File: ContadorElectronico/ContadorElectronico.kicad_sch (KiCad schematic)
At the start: 21 parts, among them J7 INPUT, J8 POWER, SW1 MODE, SW2 INC, SW3 DEC, U3 4N35, U4 4N35

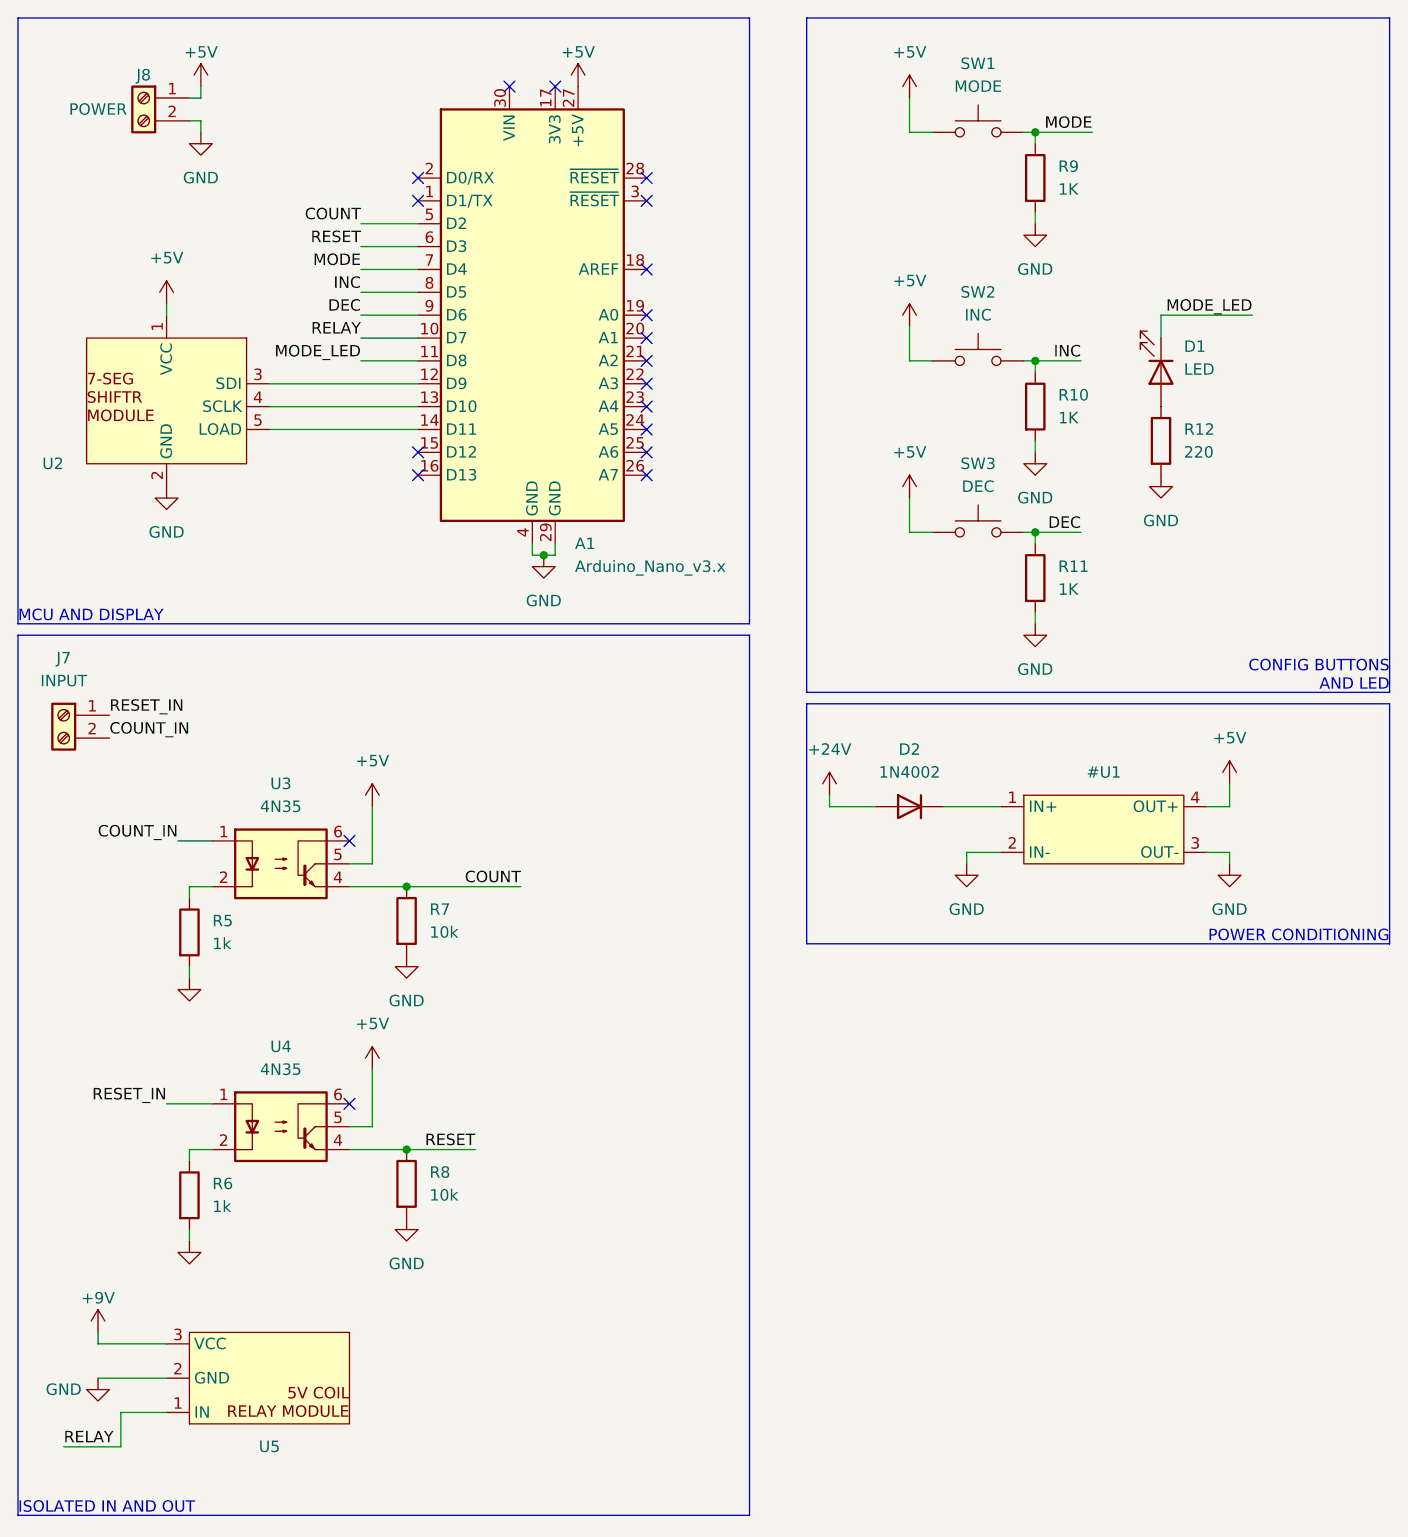
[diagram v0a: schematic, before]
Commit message: PCB design with 3 pin bornier
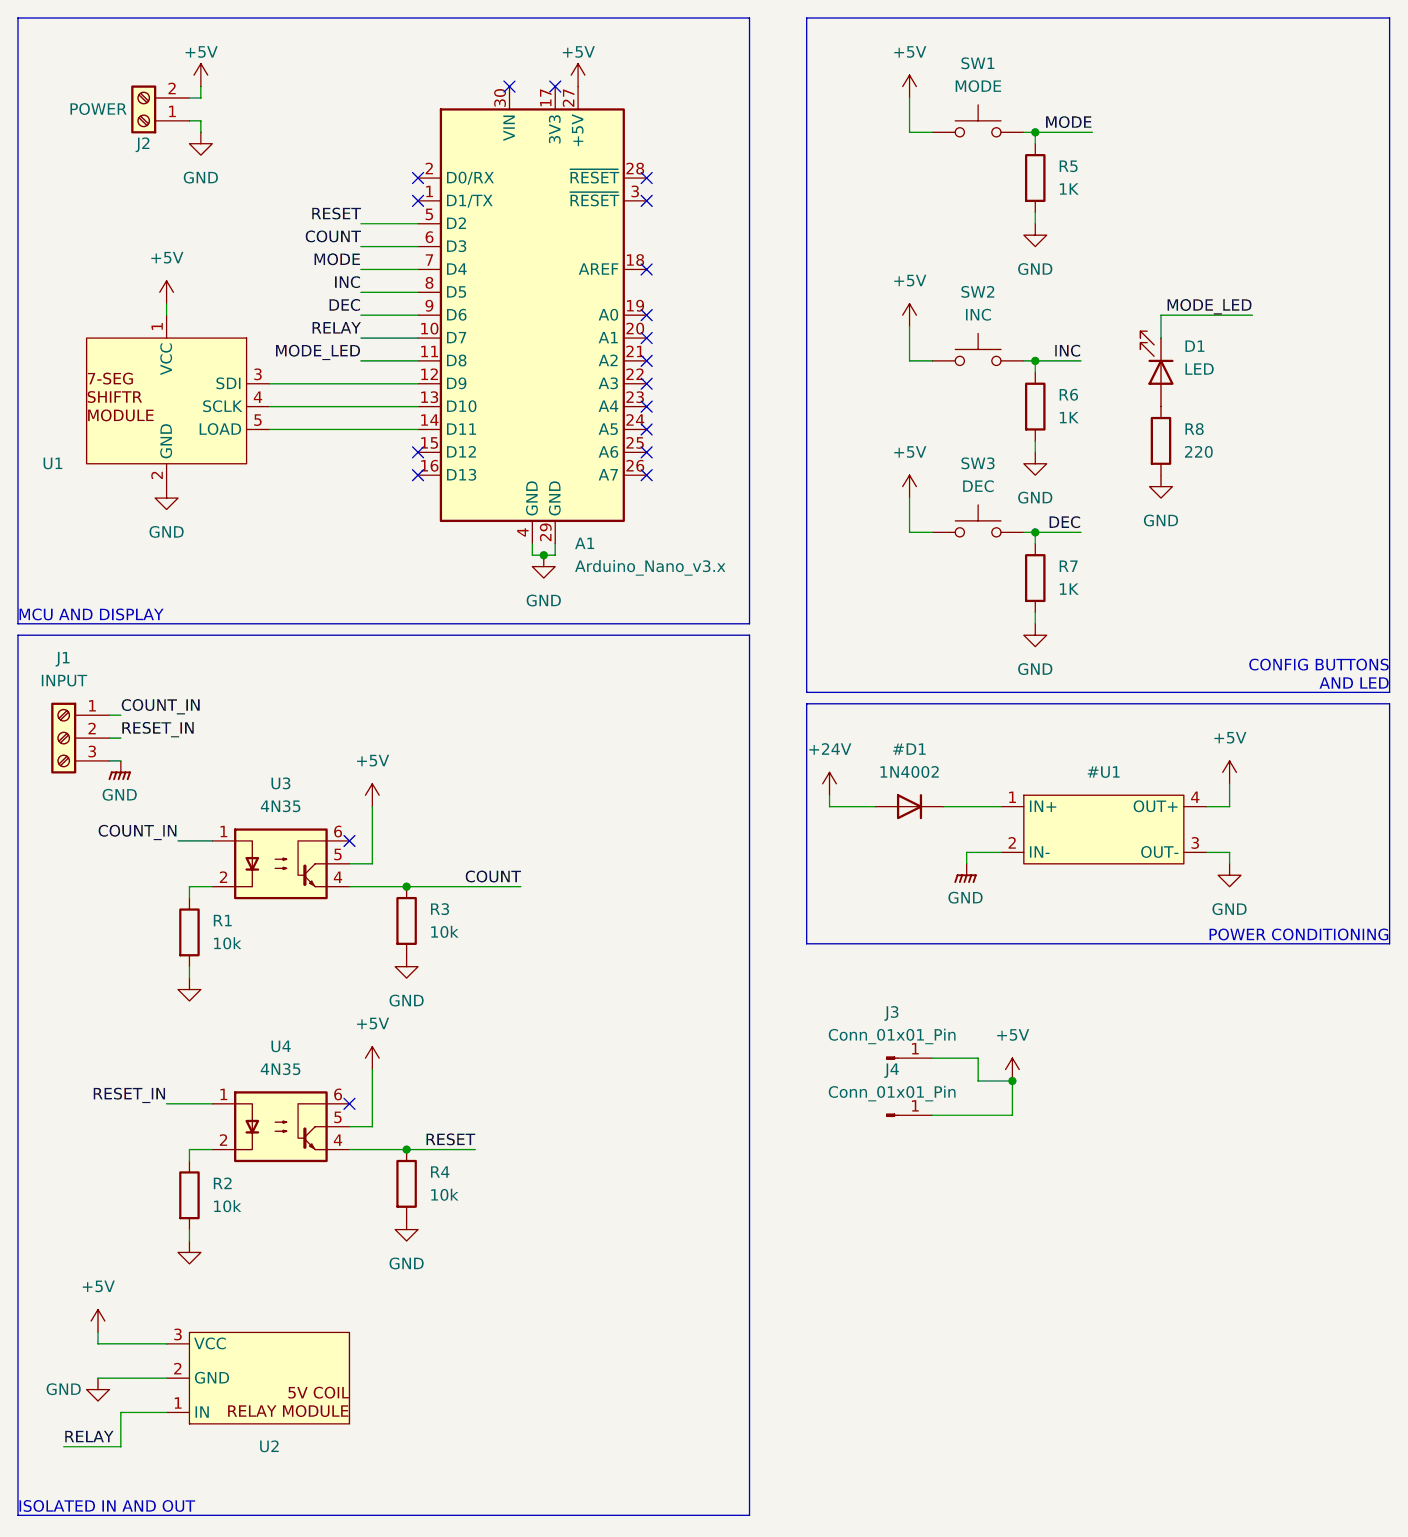
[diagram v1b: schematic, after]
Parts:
- added J3, J4: Conn_01x01_Pin, Connector_Pin:Pin_D1.3mm_L11.3mm_W2.8mm_Flat, symbol Connector:Conn_01x01_Pin
- D1, SW1, SW2, SW3: footprint Connector_PinSocket_2.54mm:PinSocket_1x02_P2.54mm_Vertical -> Connector_PinHeader_2.54mm:PinHeader_1x02_P2.54mm_Vertical
- J1: renamed from J7; footprint TerminalBlock:TerminalBlock_bornier-2_P5.08mm -> TerminalBlock:TerminalBlock_bornier-3_P5.08mm; symbol Connector:Screw_Terminal_01x02 -> Connector:Screw_Terminal_01x03
- R1: renamed from R5; value 1k -> 10k
- R2: renamed from R6; value 1k -> 10k
- U1: renamed from U2; footprint Connector_PinSocket_2.54mm:PinSocket_1x05_P2.54mm_Vertical -> Connector_PinHeader_2.54mm:PinHeader_1x05_P2.54mm_Vertical
- U2: renamed from U5; footprint Connector_PinSocket_2.54mm:PinSocket_1x03_P2.54mm_Vertical -> Connector_PinHeader_2.54mm:PinHeader_1x03_P2.54mm_Vertical
- U3, U4: footprint Package_DIP:DIP-6_W7.62mm -> Package_DIP:DIP-6_W7.62mm_Socket
- renumbered D2 to #D1, J8 to J2, R7 to R3, R8 to R4, R9 to R5, R10 to R6, R11 to R7, R12 to R8
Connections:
- net +9V is gone; now on net +5V: U2.3 (VCC)
- net +5V: now also J2.2 (Pin_2), J3.1 (Pin_1), J4.1 (Pin_1); no longer J2.1 (Pin_1)
- net COUNT: now also A1.6 (D3); no longer A1.5 (D2)
- net COUNT_IN: now also J1.1 (Pin_1); no longer J1.2 (Pin_2)
- net GND: now also J2.1 (Pin_1); no longer #U1.2 (IN-), J2.2 (Pin_2)
- net RESET: now also A1.5 (D2); no longer A1.6 (D3)
- net RESET_IN: now also J1.2 (Pin_2); no longer J1.1 (Pin_1)
- new net GNDPWR: #U1.2 (IN-), J1.3 (Pin_3)
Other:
- moved on the sheet: J2

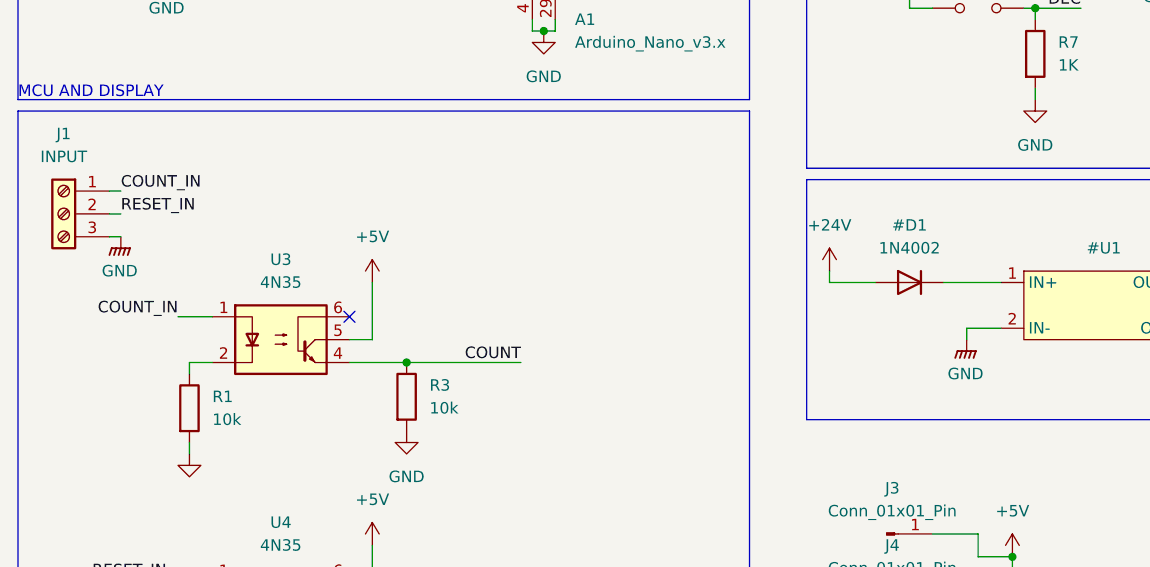
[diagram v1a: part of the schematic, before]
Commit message: 2 Pin Bornier for inputs
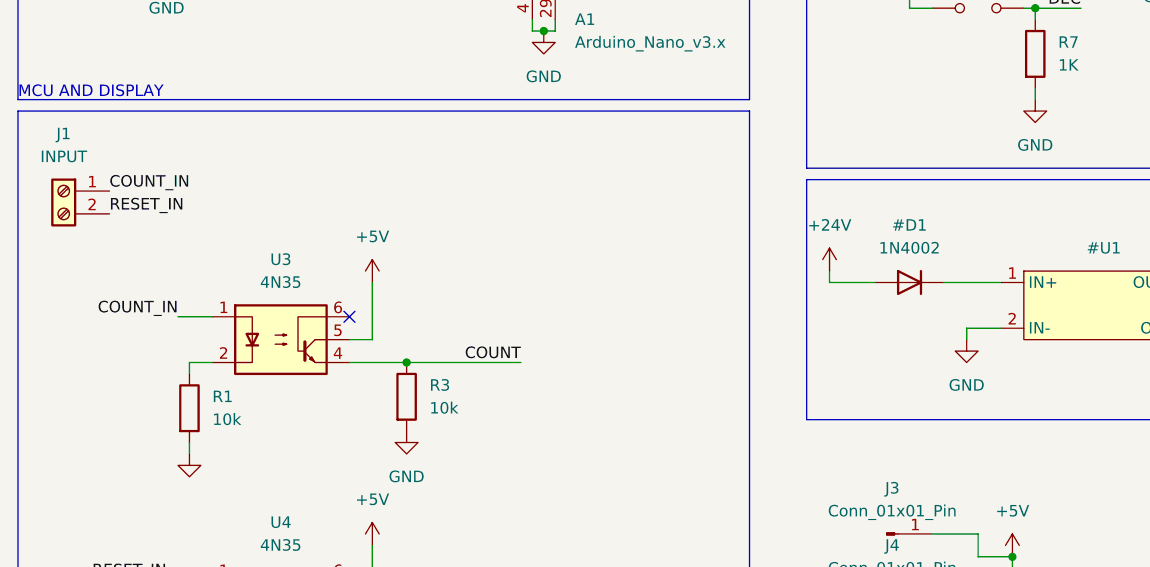
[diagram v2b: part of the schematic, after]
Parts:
- J1: footprint TerminalBlock:TerminalBlock_bornier-3_P5.08mm -> TerminalBlock:TerminalBlock_bornier-2_P5.08mm; symbol Connector:Screw_Terminal_01x03 -> Connector:Screw_Terminal_01x02
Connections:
- net GND: now also #U1.2 (IN-)
- removed net GNDPWR: #U1.2 (IN-), J1.3 (Pin_3)
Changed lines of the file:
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@@
-    (stroke (width 0) (type default))
-  )
-  (wire (pts (xy 31.75 99.06) (xy 30.48 99.06))
     (stroke (width 0) (type default))
   )
@@
     (stroke (width 0) (type default))
   )
-  (wire (pts (xy 31.75 101.6) (xy 30.48 101.6))
-    (stroke (width 0) (type default))
-  )
   (wire (pts (xy 123.19 106.68) (xy 129.54 106.68))
     (stroke (width 0) (type default))
@@
   )
   (wire (pts (xy 29.21 166.37) (xy 29.21 165.1))
-    (stroke (width 0) (type default))
-  )
-  (wire (pts (xy 31.75 96.52) (xy 30.48 96.52))
     (stroke (width 0) (type default))
   )
@@
     (effects (font (size 1.27 1.27)) (justify right bottom))
   )
-  (label "COUNT_IN" (at 31.75 96.52 0) (fields_autoplaced)
+  (label "COUNT_IN" (at 30.48 96.52 0) (fields_autoplaced)
     (effects (font (size 1.27 1.27)) (justify left bottom))
   )
@@
     (effects (font (size 1.27 1.27)) (justify right bottom))
   )
-  (label "RESET_IN" (at 31.75 99.06 0) (fields_autoplaced)
+  (label "RESET_IN" (at 30.48 99.06 0) (fields_autoplaced)
     (effects (font (size 1.27 1.27)) (justify left bottom))
   )
@@
     )
   )
-  (symbol (lib_id "power:GNDPWR") (at 125.73 113.03 0) (unit 1)
+  (symbol (lib_id "power:GND") (at 125.73 113.03 0) (unit 1)
     (in_bom yes) (on_board yes) (dnp no) (fields_autoplaced)
     (property "Reference" "#PWR019" (at 125.73 119.38 0)
       (effects (font (size 1.27 1.27)) hide)
     )
-    (property "Value" "GND" (at 125.603 116.84 0)
-      (effects (font (size 1.27 1.27)))
-    )
-    (property "Footprint" "" (at 125.73 114.3 0)
-      (effects (font (size 1.27 1.27)) hide)
-    )
-    (property "Datasheet" "" (at 125.73 114.3 0)
+    (property "Value" "GND" (at 125.73 118.11 0)
+      (effects (font (size 1.27 1.27)))
+    )
+    (property "Footprint" "" (at 125.73 113.03 0)
+      (effects (font (size 1.27 1.27)) hide)
+    )
+    (property "Datasheet" "" (at 125.73 113.03 0)
       (effects (font (size 1.27 1.27)) hide)
     )
@@
     )
   )
-  (symbol (lib_id "Connector:Screw_Terminal_01x03") (at 25.4 99.06 0) (mirror y) (unit 1)
+  (symbol (lib_id "Connector:Screw_Terminal_01x02") (at 25.4 96.52 0) (mirror y) (unit 1)
     (in_bom yes) (on_board yes) (dnp no) (fields_autoplaced)
     (property "Reference" "J1" (at 25.4 90.17 0)
@@
       (effects (font (size 1.27 1.27)))
     )
-    (property "Footprint" "TerminalBlock:TerminalBlock_bornier-3_P5.08mm" (at 25.4 99.06 0)
-      (effects (font (size 1.27 1.27)) hide)
-    )
-    (property "Datasheet" "~" (at 25.4 99.06 0)
-      (effects (font (size 1.27 1.27)) hide)
-    )
-    (pin "1")
-    (pin "2")
-    (pin "3")
+    (property "Footprint" "TerminalBlock:TerminalBlock_bornier-2_P5.08mm" (at 25.4 96.52 0)
+      (effects (font (size 1.27 1.27)) hide)
+    )
+    (property "Datasheet" "~" (at 25.4 96.52 0)
+      (effects (font (size 1.27 1.27)) hide)
+    )
+    (pin "1")
+    (pin "2")
     (instances
       (project "ContadorElectronico"
@@
         )
       )
-    )
-  )
-  (symbol (lib_id "power:GNDPWR") (at 31.75 101.6 0) (unit 1)
-    (in_bom yes) (on_board yes) (dnp no) (fields_autoplaced)
-    (property "Reference" "#PWR027" (at 31.75 107.95 0)
-      (effects (font (size 1.27 1.27)) hide)
-    )
-    (property "Value" "GND" (at 31.623 105.41 0)
-      (effects (font (size 1.27 1.27)))
-    )
-    (property "Footprint" "" (at 31.75 102.87 0)
-      (effects (font (size 1.27 1.27)) hide)
-    )
-    (property "Datasheet" "" (at 31.75 102.87 0)
-      (effects (font (size 1.27 1.27)) hide)
-    )
-    (pin "1")
-    (instances
-      (project "ContadorElectronico"
-        (path "/7e60630a-8ace-4264-b872-1b7f6bc0698d"
-          (reference "#PWR027") (unit 1)
-        )
-      )

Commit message: Cambios varios
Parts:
- R1, R2, R3, R4, R5, R6, R7, R8: footprint Resistor_THT:R_Axial_DIN0207_L6.3mm_D2.5mm_P10.16mm_Horizontal -> Resistor_SMD:R_1206_3216Metric
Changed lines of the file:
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@@
       (effects (font (size 1.27 1.27)) (justify left))
     )
-    (property "Footprint" "Resistor_THT:R_Axial_DIN0207_L6.3mm_D2.5mm_P10.16mm_Horizontal" (at 131.572 81.28 90)
+    (property "Footprint" "Resistor_SMD:R_1206_3216Metric" (at 131.572 81.28 90)
       (effects (font (size 1.27 1.27)) hide)
     )
@@
       (effects (font (size 1.27 1.27)) (justify left))
     )
-    (property "Footprint" "Resistor_THT:R_Axial_DIN0207_L6.3mm_D2.5mm_P10.16mm_Horizontal" (at 61.722 148.59 90)
+    (property "Footprint" "Resistor_SMD:R_1206_3216Metric" (at 61.722 148.59 90)
       (effects (font (size 1.27 1.27)) hide)
     )
@@
       (effects (font (size 1.27 1.27)) (justify left))
     )
-    (property "Footprint" "Resistor_THT:R_Axial_DIN0207_L6.3mm_D2.5mm_P10.16mm_Horizontal" (at 61.722 119.38 90)
+    (property "Footprint" "Resistor_SMD:R_1206_3216Metric" (at 61.722 119.38 90)
       (effects (font (size 1.27 1.27)) hide)
     )
@@
       (effects (font (size 1.27 1.27)) (justify left))
     )
-    (property "Footprint" "Resistor_THT:R_Axial_DIN0207_L6.3mm_D2.5mm_P10.16mm_Horizontal" (at 131.572 36.83 90)
+    (property "Footprint" "Resistor_SMD:R_1206_3216Metric" (at 131.572 36.83 90)
       (effects (font (size 1.27 1.27)) hide)
     )
@@
       (effects (font (size 1.27 1.27)) (justify left))
     )
-    (property "Footprint" "Resistor_THT:R_Axial_DIN0207_L6.3mm_D2.5mm_P10.16mm_Horizontal" (at 37.592 149.86 90)
+    (property "Footprint" "Resistor_SMD:R_1206_3216Metric" (at 37.592 149.86 90)
       (effects (font (size 1.27 1.27)) hide)
     )
@@
       (effects (font (size 1.27 1.27)) (justify left))
     )
-    (property "Footprint" "Resistor_THT:R_Axial_DIN0207_L6.3mm_D2.5mm_P10.16mm_Horizontal" (at 131.572 62.23 90)
+    (property "Footprint" "Resistor_SMD:R_1206_3216Metric" (at 131.572 62.23 90)
       (effects (font (size 1.27 1.27)) hide)
     )
@@
       (effects (font (size 1.27 1.27)) (justify left))
     )
-    (property "Footprint" "Resistor_THT:R_Axial_DIN0207_L6.3mm_D2.5mm_P10.16mm_Horizontal" (at 37.592 120.65 90)
+    (property "Footprint" "Resistor_SMD:R_1206_3216Metric" (at 37.592 120.65 90)
       (effects (font (size 1.27 1.27)) hide)
     )
@@
       (effects (font (size 1.27 1.27)) (justify left))
     )
-    (property "Footprint" "Resistor_THT:R_Axial_DIN0207_L6.3mm_D2.5mm_P10.16mm_Horizontal" (at 145.542 66.04 90)
-      (effects (font (size 1.27 1.27)) hide)
-    )
+    (property "Footprint" "Resistor_SMD:R_1206_3216Metric" (at 145.542 66.04 90)
+      (effects (font (size 1.27 1.27)) hide)
+    )
